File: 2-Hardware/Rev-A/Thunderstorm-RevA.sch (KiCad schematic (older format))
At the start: 16 parts

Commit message: Changed humidity sensor part number to be correct (fixes #1). Updated op-amp circuit to fix incorrect negative terminal wiring (fixes #3). Changed ADC input for humidity sensor to connect Vref to Vcc (fixes #2). Added bulk decoupling capacitor on the Synapse module.
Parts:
- added C4: 0.1uF, ~, symbol C
- A2: renamed from A?; value HIH_3030 -> HIH_5030; symbol HIH_3030 -> HIH_5030
- gave numbers to parts that had none: 15
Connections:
- net labels added: ADC3
- net labels removed: ADC0
- wire segments 89 -> 94
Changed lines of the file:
@@
 LIBS:Sensors
 LIBS:TransistorParts
+LIBS:Thunderstorm-RevA-cache
 EELAYER 27 0
 EELAYER END
@@
 Sheet 1 1
 Title ""
-Date "20 may 2014"
+Date "27 may 2014"
 Rev ""
 Comp ""
@@
 $EndDescr
 $Comp
-L SYNAPSE_RF300 RF?
+L SYNAPSE_RF300 RF1
 U 1 1 537AB6CF
 P 2850 6550
-F 0 "RF?" H 2850 7250 60  0000 C CNN
+F 0 "RF1" H 2850 7250 60  0000 C CNN
 F 1 "SYNAPSE_RF300" H 2900 7350 60  0000 C CNN
 F 2 "~" H 2850 6550 60  0000 C CNN
@@
 $EndComp
 $Comp
-L BATTERY BT?
+L BATTERY BT1
 U 1 1 537AB6DE
 P 9600 4050
-F 0 "BT?" H 9600 4250 50  0000 C CNN
+F 0 "BT1" H 9600 4250 50  0000 C CNN
 F 1 "BATTERY" H 9600 3860 50  0000 C CNN
 F 2 "~" H 9600 4050 60  0000 C CNN
@@
 $EndComp
 $Comp
-L SWITCH_SPDT SW?
+L SWITCH_SPDT SW1
 U 1 1 537AB6ED
 P 10300 4050
-F 0 "SW?" H 10300 4200 50  0000 C CNN
+F 0 "SW1" H 10300 4200 50  0000 C CNN
 F 1 "SWITCH_SPDT" H 10300 3950 50  0000 C CNN
 F 2 "~" H 10300 4050 60  0000 C CNN
@@
 $EndComp
 $Comp
-L GND #PWR?
+L GND #PWR11
 U 1 1 537AB6FC
 P 9200 4150
-F 0 "#PWR?" H 9200 4150 30  0001 C CNN
+F 0 "#PWR11" H 9200 4150 30  0001 C CNN
 F 1 "GND" H 9200 4080 30  0001 C CNN
 F 2 "" H 9200 4150 60  0000 C CNN
@@
 	10600 4000 10600 3950
 $Comp
-L +BATT #PWR?
+L +BATT #PWR14
 U 1 1 537AB71B
 P 10600 3950
-F 0 "#PWR?" H 10600 3900 20  0001 C CNN
+F 0 "#PWR14" H 10600 3900 20  0001 C CNN
 F 1 "+BATT" H 10600 4050 30  0000 C CNN
 F 2 "" H 10600 3950 60  0000 C CNN
@@
 $EndComp
 $Comp
-L +BATT #PWR?
+L +BATT #PWR5
 U 1 1 537AB72A
 P 4050 6000
-F 0 "#PWR?" H 4050 5950 20  0001 C CNN
+F 0 "#PWR5" H 4050 5950 20  0001 C CNN
 F 1 "+BATT" H 4050 6100 30  0000 C CNN
 F 2 "" H 4050 6000 60  0000 C CNN
@@
 	4050 6300 3400 6300
 $Comp
-L GND #PWR?
+L GND #PWR4
 U 1 1 537AB73F
 P 3600 5900
-F 0 "#PWR?" H 3600 5900 30  0001 C CNN
+F 0 "#PWR4" H 3600 5900 30  0001 C CNN
 F 1 "GND" H 3600 5830 30  0001 C CNN
 F 2 "" H 3600 5900 60  0000 C CNN
@@
 $EndComp
 $Comp
-L GND #PWR?
+L GND #PWR3
 U 1 1 537AB74E
 P 2050 5950
-F 0 "#PWR?" H 2050 5950 30  0001 C CNN
+F 0 "#PWR3" H 2050 5950 30  0001 C CNN
 F 1 "GND" H 2050 5880 30  0001 C CNN
 F 2 "" H 2050 5950 60  0000 C CNN
@@
 $EndComp
 $Comp
-L R R?
+L R R3
 U 1 1 537AB784
 P 3750 6100
-F 0 "R?" V 3830 6100 40  0000 C CNN
+F 0 "R3" V 3830 6100 40  0000 C CNN
 F 1 "4.7k" V 3757 6101 40  0000 C CNN
 F 2 "~" V 3680 6100 30  0000 C CNN
@@
 	2050 5900 2050 5950
 $Comp
-L R R?
+L R R1
 U 1 1 537AB7FB
 P 1500 5750
-F 0 "R?" V 1580 5750 40  0000 C CNN
+F 0 "R1" V 1580 5750 40  0000 C CNN
 F 1 "4.7k" V 1507 5751 40  0000 C CNN
 F 2 "~" V 1430 5750 30  0000 C CNN
@@
 $EndComp
 $Comp
-L R R?
+L R R2
 U 1 1 537AB80A
 P 1700 5750
-F 0 "R?" V 1780 5750 40  0000 C CNN
+F 0 "R2" V 1780 5750 40  0000 C CNN
 F 1 "4.7k" V 1707 5751 40  0000 C CNN
 F 2 "~" V 1630 5750 30  0000 C CNN
@@
 $EndComp
 $Comp
-L +BATT #PWR?
+L +BATT #PWR1
 U 1 1 537AB819
 P 1600 5400
-F 0 "#PWR?" H 1600 5350 20  0001 C CNN
+F 0 "#PWR1" H 1600 5350 20  0001 C CNN
 F 1 "+BATT" H 1600 5500 30  0000 C CNN
 F 2 "" H 1600 5400 60  0000 C CNN
@@
 Text Label 1400 6200 2    60   ~ 0
 SCL
-Text Label 1900 6700 2    60   ~ 0
-ADC0
-Wire Wire Line
-	2300 6700 1900 6700
+Text Label 1900 7000 2    60   ~ 0
+ADC3
 Text Label 1900 6800 2    60   ~ 0
 USART_RF_RXI
@@
 	2300 6800 1900 6800
 $Comp
-L M10382 U?
+L M10382 U1
 U 1 1 537AB9A1
 P 9100 2250
-F 0 "U?" H 9100 2300 60  0000 C CNN
+F 0 "U1" H 9100 2300 60  0000 C CNN
 F 1 "M10382" H 9100 2200 60  0000 C CNN
 F 2 "~" H 9100 2250 60  0000 C CNN
@@
 $EndComp
 $Comp
-L GND #PWR?
+L GND #PWR10
 U 1 1 537AB9B0
 P 9100 3050
-F 0 "#PWR?" H 9100 3050 30  0001 C CNN
+F 0 "#PWR10" H 9100 3050 30  0001 C CNN
 F 1 "GND" H 9100 2980 30  0001 C CNN
 F 2 "" H 9100 3050 60  0000 C CNN
@@
 Connection ~ 9550 2950
 $Comp
-L +BATT #PWR?
+L +BATT #PWR9
 U 1 1 537ABBDB
 P 7400 1850
-F 0 "#PWR?" H 7400 1800 20  0001 C CNN
+F 0 "#PWR9" H 7400 1800 20  0001 C CNN
 F 1 "+BATT" H 7400 1950 30  0000 C CNN
 F 2 "" H 7400 1850 60  0000 C CNN
@@
 Connection ~ 7400 2150
 $Comp
-L C C?
+L C C1
 U 1 1 537ABC6A
 P 7400 2650
-F 0 "C?" H 7400 2750 40  0000 L CNN
+F 0 "C1" H 7400 2750 40  0000 L CNN
 F 1 "22pF" H 7406 2565 40  0000 L CNN
 F 2 "~" H 7438 2500 30  0000 C CNN
@@
 Connection ~ 7400 2350
 $Comp
-L C C?
+L C C2
 U 1 1 537ABD23
 P 10750 2250
-F 0 "C?" H 10750 2350 40  0000 L CNN
+F 0 "C2" H 10750 2350 40  0000 L CNN
 F 1 "22pF" H 10756 2165 40  0000 L CNN
 F 2 "~" H 10788 2100 30  0000 C CNN
@@
 	9200 1550 9200 1650
 $Comp
-L HIH_3030 A?
+L HIH_5030 A2
 U 1 1 537AC044
 P 10450 5550
-F 0 "A?" H 10450 5800 60  0000 C CNN
-F 1 "HIH_3030" H 10450 5650 60  0000 C CNN
+F 0 "A2" H 10450 5800 60  0000 C CNN
+F 1 "HIH_5030" H 10450 5650 60  0000 C CNN
 F 2 "" H 10350 5500 60  0000 C CNN
 F 3 "" H 10350 5500 60  0000 C CNN
@@
 $EndComp
 $Comp
-L LM358 U?
+L LM358 U2
 U 1 1 537AC053
 P 9200 6200
-F 0 "U?" H 9150 6400 60  0000 L CNN
+F 0 "U2" H 9150 6400 60  0000 L CNN
 F 1 "LM358" H 9150 5950 60  0000 L CNN
 F 2 "" H 9200 6200 60  0000 C CNN
@@
 	10450 6100 9700 6100
 $Comp
-L R R?
+L R R6
 U 1 1 537AC0BB
 P 10050 6400
-F 0 "R?" V 10130 6400 40  0000 C CNN
+F 0 "R6" V 10130 6400 40  0000 C CNN
 F 1 "68k" V 10057 6401 40  0000 C CNN
 F 2 "~" V 9980 6400 30  0000 C CNN
@@
 	9700 6300 9800 6300
 Wire Wire Line
-	9800 6300 9800 6650
-Wire Wire Line
 	9300 6650 10850 6650
 Wire Wire Line
@@
 Connection ~ 10050 6650
 $Comp
-L GND #PWR?
+L GND #PWR13
 U 1 1 537AC1B6
 P 10050 6750
-F 0 "#PWR?" H 10050 6750 30  0001 C CNN
+F 0 "#PWR13" H 10050 6750 30  0001 C CNN
 F 1 "GND" H 10050 6680 30  0001 C CNN
 F 2 "" H 10050 6750 60  0000 C CNN
@@
 	10050 6650 10050 6750
 $Comp
-L +BATT #PWR?
+L +BATT #PWR15
 U 1 1 537AC216
 P 10850 5800
-F 0 "#PWR?" H 10850 5750 20  0001 C CNN
+F 0 "#PWR15" H 10850 5750 20  0001 C CNN
 F 1 "+BATT" H 10850 5900 30  0000 C CNN
 F 2 "" H 10850 5800 60  0000 C CNN
@@
 $EndComp
 $Comp
-L +BATT #PWR?
+L +BATT #PWR12
 U 1 1 537AC225
 P 9300 5700
-F 0 "#PWR?" H 9300 5650 20  0001 C CNN
+F 0 "#PWR12" H 9300 5650 20  0001 C CNN
 F 1 "+BATT" H 9300 5800 30  0000 C CNN
 F 2 "" H 9300 5700 60  0000 C CNN
@@
 Wire Wire Line
 	9300 6600 9300 6650
-Connection ~ 9800 6650
 Wire Wire Line
 	10050 6150 10050 6100
@@
 	10850 5800 10850 6150
 Text Label 8600 6200 2    60   ~ 0
-ADC0
+ADC3
 Wire Wire Line
 	8700 6200 8600 6200
@@
 Power
 $Comp
-L C C?
+L C C3
 U 1 1 537AC660
 P 10850 6350
-F 0 "C?" H 10850 6450 40  0000 L CNN
+F 0 "C3" H 10850 6450 40  0000 L CNN
 F 1 "0.1uF" H 10856 6265 40  0000 L CNN
 F 2 "~" H 10888 6200 30  0000 C CNN
@@
 Connection ~ 10850 5850
 $Comp
-L LPS331AP A?
+L LPS331AP A1
 U 1 1 537ACB3D
 P 6750 6200
-F 0 "A?" H 6300 6700 60  0000 C CNN
+F 0 "A1" H 6300 6700 60  0000 C CNN
 F 1 "LPS331AP" H 7200 5700 60  0000 C CNN
 F 2 "" H 6900 6000 60  0000 C CNN
@@
 $EndComp
 $Comp
-L GND #PWR?
+L GND #PWR8
 U 1 1 537ACB4C
 P 6750 7050
-F 0 "#PWR?" H 6750 7050 30  0001 C CNN
+F 0 "#PWR8" H 6750 7050 30  0001 C CNN
 F 1 "GND" H 6750 6980 30  0001 C CNN
 F 2 "" H 6750 7050 60  0000 C CNN
@@
 Connection ~ 6650 6950
 $Comp
-L R R?
+L R R4
 U 1 1 537ACDDA
 P 7550 5750
-F 0 "R?" V 7630 5750 40  0000 C CNN
+F 0 "R4" V 7630 5750 40  0000 C CNN
 F 1 "4.7k" V 7557 5751 40  0000 C CNN
 F 2 "~" V 7480 5750 30  0000 C CNN
@@
 	6750 5350 6750 5650
 $Comp
-L +BATT #PWR?
+L +BATT #PWR7
 U 1 1 537ACEB8
 P 6750 5350
-F 0 "#PWR?" H 6750 5300 20  0001 C CNN
+F 0 "#PWR7" H 6750 5300 20  0001 C CNN
 F 1 "+BATT" H 6750 5450 30  0000 C CNN
 F 2 "" H 6750 5350 60  0000 C CNN
@@
 Connection ~ 6950 6950
 $Comp
-L R R?
+L R R5
 U 1 1 537AD31D
 P 7650 6650
-F 0 "R?" V 7730 6650 40  0000 C CNN
+F 0 "R5" V 7730 6650 40  0000 C CNN
 F 1 "4.7k" V 7657 6651 40  0000 C CNN
 F 2 "~" V 7580 6650 30  0000 C CNN
@@
 Wire Notes Line
 	6950 3350 6950 500
+Wire Wire Line
+	9800 6300 9800 6750
+Wire Wire Line
+	9800 6750 8650 6750
+Wire Wire Line
+	8650 6750 8650 6200
+Connection ~ 8650 6200
+$Comp
+L +BATT #PWR2
+U 1 1 53851E13
+P 1800 6650
+F 0 "#PWR2" H 1800 6600 20  0001 C CNN
+F 1 "+BATT" H 1800 6750 30  0000 C CNN
+F 2 "" H 1800 6650 60  0000 C CNN
+F 3 "" H 1800 6650 60  0000 C CNN
+	1    1800 6650
+	1    0    0    -1
+$EndComp
+Wire Wire Line
+	2300 6700 1800 6700
+Wire Wire Line
+	1800 6700 1800 6650
+Wire Wire Line
+	1900 7000 2300 7000
+$Comp
+L C C4
+U 1 1 53852370
+P 4050 6500
+F 0 "C4" H 4050 6600 40  0000 L CNN
+F 1 "0.1uF" H 4056 6415 40  0000 L CNN
+F 2 "~" H 4088 6350 30  0000 C CNN
+F 3 "~" H 4050 6500 60  0000 C CNN
+	1    4050 6500
+	1    0    0    -1
+$EndComp
+$Comp
+L GND #PWR6
+U 1 1 5385237F
+P 4050 6800
+F 0 "#PWR6" H 4050 6800 30  0001 C CNN
+F 1 "GND" H 4050 6730 30  0001 C CNN
+F 2 "" H 4050 6800 60  0000 C CNN
+F 3 "" H 4050 6800 60  0000 C CNN
+	1    4050 6800
+	1    0    0    -1
+$EndComp
+Wire Wire Line
+	4050 6700 4050 6800
 $EndSCHEMATC

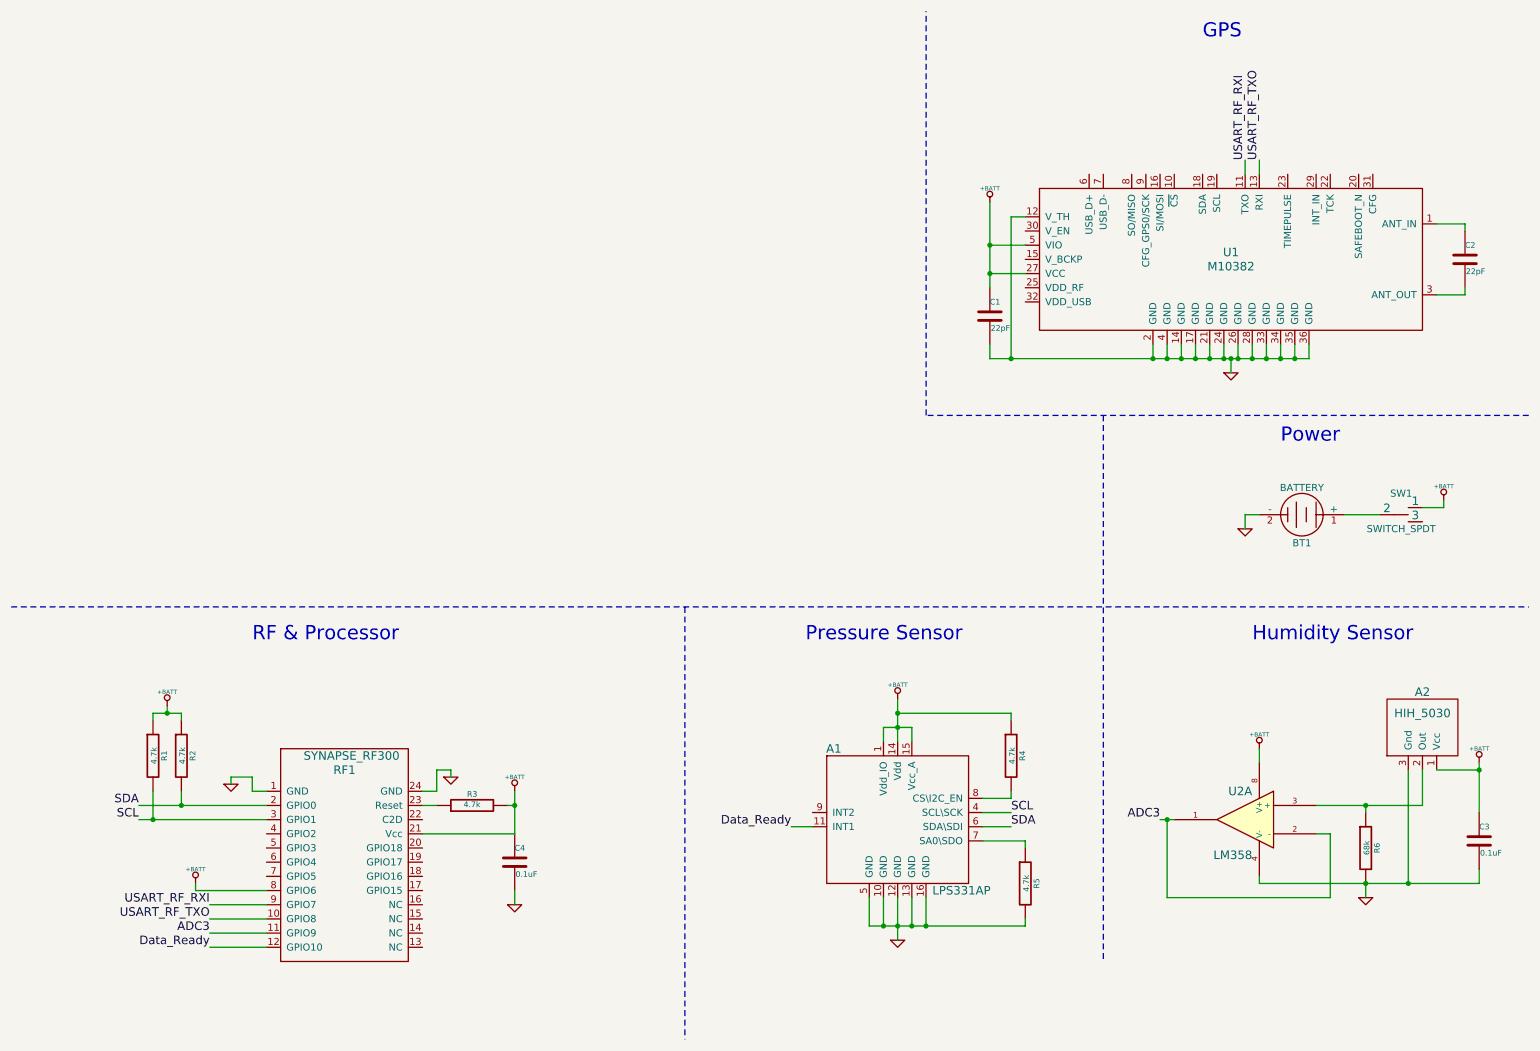
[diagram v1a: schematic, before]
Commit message: Added LEDs for power and diagnostics. (Fixes #4).
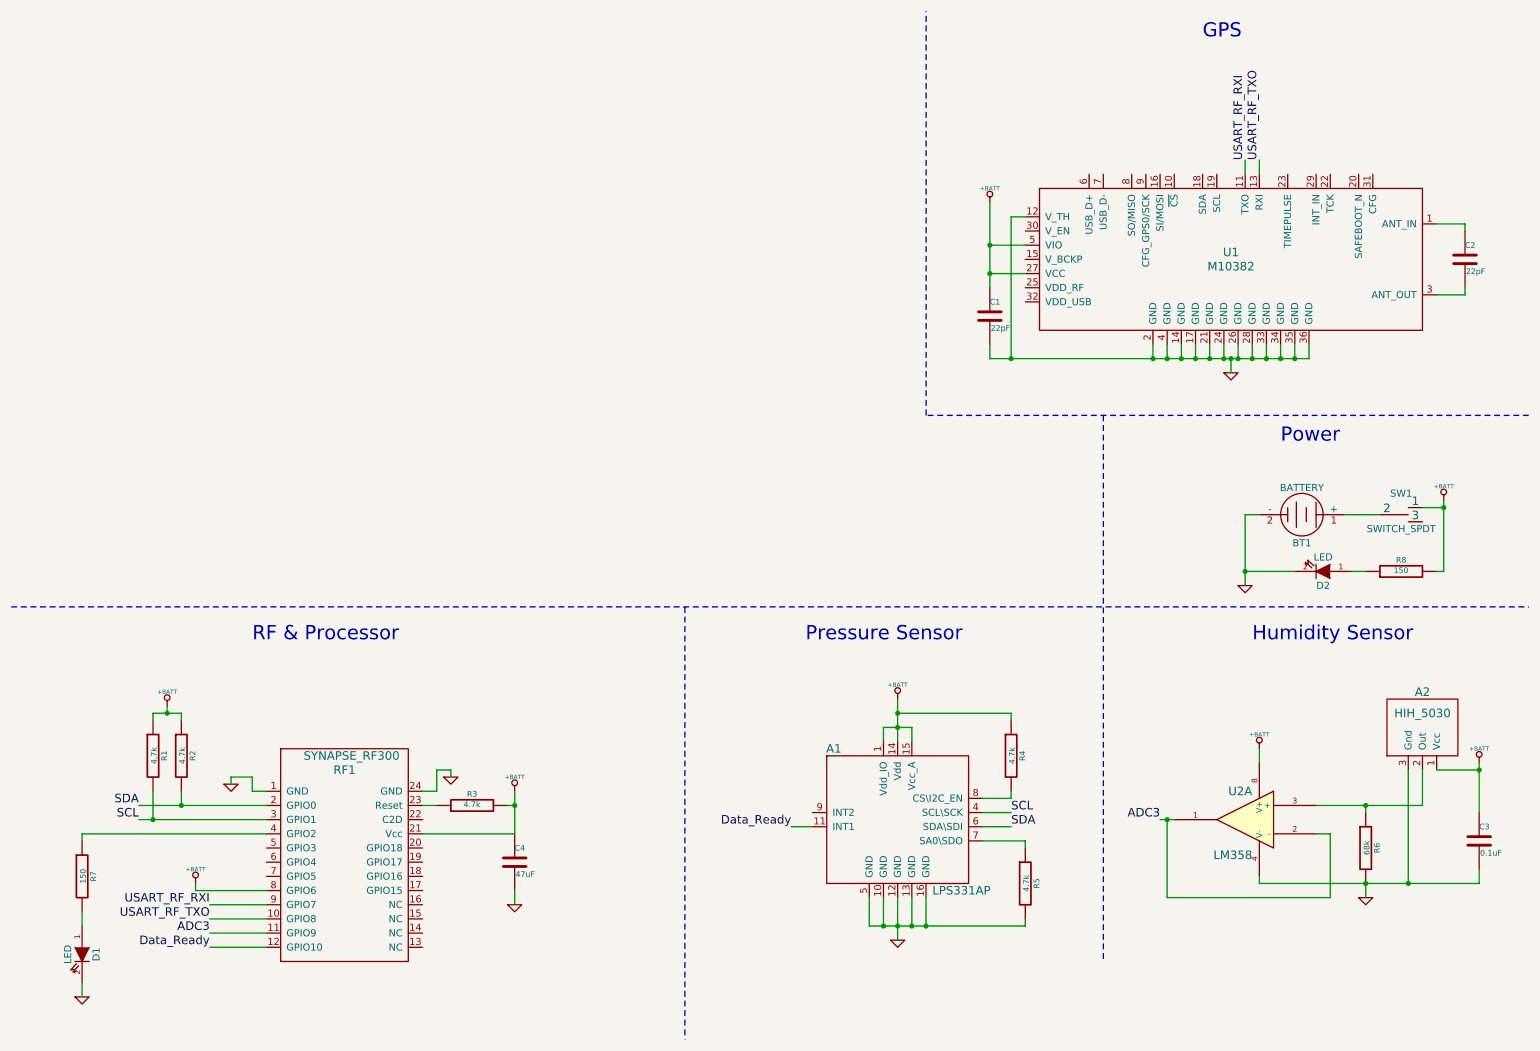
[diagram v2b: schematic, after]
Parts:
- added D1, D2: LED, ~, symbol LED
- added R7, R8: 150, ~, symbol R
- C4: value 0.1uF -> 47uF
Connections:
- net +BATT: now also R8.2
- net GND: now also D1.2 (K), D2.2 (K)
- net at RF1.4 (GPIO2): now also R7.1
- new net: D2.1 (A), R8.1
- new net: D1.1 (A), R7.2
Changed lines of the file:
@@
 Sheet 1 1
 Title ""
-Date "27 may 2014"
+Date "28 may 2014"
 Rev ""
 Comp ""
@@
 $EndComp
 $Comp
-L GND #PWR11
+L GND #PWR12
 U 1 1 537AB6FC
-P 9200 4150
-F 0 "#PWR11" H 9200 4150 30  0001 C CNN
-F 1 "GND" H 9200 4080 30  0001 C CNN
-F 2 "" H 9200 4150 60  0000 C CNN
-F 3 "" H 9200 4150 60  0000 C CNN
-	1    9200 4150
+P 9200 4550
+F 0 "#PWR12" H 9200 4550 30  0001 C CNN
+F 1 "GND" H 9200 4480 30  0001 C CNN
+F 2 "" H 9200 4550 60  0000 C CNN
+F 3 "" H 9200 4550 60  0000 C CNN
+	1    9200 4550
 	1    0    0    -1
 $EndComp
@@
 	9300 4050 9200 4050
 Wire Wire Line
-	9200 4050 9200 4150
+	9200 4050 9200 4550
 Wire Wire Line
 	9900 4050 10150 4050
@@
 	10450 4000 10600 4000
 Wire Wire Line
-	10600 4000 10600 3950
-$Comp
-L +BATT #PWR14
+	10600 3950 10600 4450
+$Comp
+L +BATT #PWR15
 U 1 1 537AB71B
 P 10600 3950
-F 0 "#PWR14" H 10600 3900 20  0001 C CNN
+F 0 "#PWR15" H 10600 3900 20  0001 C CNN
 F 1 "+BATT" H 10600 4050 30  0000 C CNN
 F 2 "" H 10600 3950 60  0000 C CNN
@@
 $EndComp
 $Comp
-L +BATT #PWR5
+L +BATT #PWR6
 U 1 1 537AB72A
 P 4050 6000
-F 0 "#PWR5" H 4050 5950 20  0001 C CNN
+F 0 "#PWR6" H 4050 5950 20  0001 C CNN
 F 1 "+BATT" H 4050 6100 30  0000 C CNN
 F 2 "" H 4050 6000 60  0000 C CNN
@@
 	4050 6300 3400 6300
 $Comp
-L GND #PWR4
+L GND #PWR5
 U 1 1 537AB73F
 P 3600 5900
-F 0 "#PWR4" H 3600 5900 30  0001 C CNN
+F 0 "#PWR5" H 3600 5900 30  0001 C CNN
 F 1 "GND" H 3600 5830 30  0001 C CNN
 F 2 "" H 3600 5900 60  0000 C CNN
@@
 $EndComp
 $Comp
-L GND #PWR3
+L GND #PWR4
 U 1 1 537AB74E
 P 2050 5950
-F 0 "#PWR3" H 2050 5950 30  0001 C CNN
+F 0 "#PWR4" H 2050 5950 30  0001 C CNN
 F 1 "GND" H 2050 5880 30  0001 C CNN
 F 2 "" H 2050 5950 60  0000 C CNN
@@
 $EndComp
 $Comp
-L +BATT #PWR1
+L +BATT #PWR2
 U 1 1 537AB819
 P 1600 5400
-F 0 "#PWR1" H 1600 5350 20  0001 C CNN
+F 0 "#PWR2" H 1600 5350 20  0001 C CNN
 F 1 "+BATT" H 1600 5500 30  0000 C CNN
 F 2 "" H 1600 5400 60  0000 C CNN
@@
 $EndComp
 $Comp
-L GND #PWR10
+L GND #PWR11
 U 1 1 537AB9B0
 P 9100 3050
-F 0 "#PWR10" H 9100 3050 30  0001 C CNN
+F 0 "#PWR11" H 9100 3050 30  0001 C CNN
 F 1 "GND" H 9100 2980 30  0001 C CNN
 F 2 "" H 9100 3050 60  0000 C CNN
@@
 Connection ~ 9550 2950
 $Comp
-L +BATT #PWR9
+L +BATT #PWR10
 U 1 1 537ABBDB
 P 7400 1850
-F 0 "#PWR9" H 7400 1800 20  0001 C CNN
+F 0 "#PWR10" H 7400 1800 20  0001 C CNN
 F 1 "+BATT" H 7400 1950 30  0000 C CNN
 F 2 "" H 7400 1850 60  0000 C CNN
@@
 $EndComp
 Wire Wire Line
-	10450 5850 10450 6100
-Wire Wire Line
-	10450 6100 9700 6100
+	10450 6100 10450 5850
+Wire Wire Line
+	9700 6100 10450 6100
 $Comp
 L R R6
@@
 Connection ~ 10050 6650
 $Comp
-L GND #PWR13
+L GND #PWR14
 U 1 1 537AC1B6
 P 10050 6750
-F 0 "#PWR13" H 10050 6750 30  0001 C CNN
+F 0 "#PWR14" H 10050 6750 30  0001 C CNN
 F 1 "GND" H 10050 6680 30  0001 C CNN
 F 2 "" H 10050 6750 60  0000 C CNN
@@
 	10050 6650 10050 6750
 $Comp
-L +BATT #PWR15
+L +BATT #PWR16
 U 1 1 537AC216
 P 10850 5800
-F 0 "#PWR15" H 10850 5750 20  0001 C CNN
+F 0 "#PWR16" H 10850 5750 20  0001 C CNN
 F 1 "+BATT" H 10850 5900 30  0000 C CNN
 F 2 "" H 10850 5800 60  0000 C CNN
@@
 $EndComp
 $Comp
-L +BATT #PWR12
+L +BATT #PWR13
 U 1 1 537AC225
 P 9300 5700
-F 0 "#PWR12" H 9300 5650 20  0001 C CNN
+F 0 "#PWR13" H 9300 5650 20  0001 C CNN
 F 1 "+BATT" H 9300 5800 30  0000 C CNN
 F 2 "" H 9300 5700 60  0000 C CNN
@@
 ADC3
 Wire Wire Line
-	8700 6200 8600 6200
+	8600 6200 8700 6200
 Text Notes 9250 4950 0    100  ~ 0
 Humidity Sensor
@@
 $EndComp
 $Comp
-L GND #PWR8
+L GND #PWR9
 U 1 1 537ACB4C
 P 6750 7050
-F 0 "#PWR8" H 6750 7050 30  0001 C CNN
+F 0 "#PWR9" H 6750 7050 30  0001 C CNN
 F 1 "GND" H 6750 6980 30  0001 C CNN
 F 2 "" H 6750 7050 60  0000 C CNN
@@
 	6750 5350 6750 5650
 $Comp
-L +BATT #PWR7
+L +BATT #PWR8
 U 1 1 537ACEB8
 P 6750 5350
-F 0 "#PWR7" H 6750 5300 20  0001 C CNN
+F 0 "#PWR8" H 6750 5300 20  0001 C CNN
 F 1 "+BATT" H 6750 5450 30  0000 C CNN
 F 2 "" H 6750 5350 60  0000 C CNN
@@
 Connection ~ 8650 6200
 $Comp
-L +BATT #PWR2
+L +BATT #PWR3
 U 1 1 53851E13
 P 1800 6650
-F 0 "#PWR2" H 1800 6600 20  0001 C CNN
+F 0 "#PWR3" H 1800 6600 20  0001 C CNN
 F 1 "+BATT" H 1800 6750 30  0000 C CNN
 F 2 "" H 1800 6650 60  0000 C CNN
@@
 P 4050 6500
 F 0 "C4" H 4050 6600 40  0000 L CNN
-F 1 "0.1uF" H 4056 6415 40  0000 L CNN
+F 1 "47uF" H 4056 6415 40  0000 L CNN
 F 2 "~" H 4088 6350 30  0000 C CNN
 F 3 "~" H 4050 6500 60  0000 C CNN
@@
 $EndComp
 $Comp
-L GND #PWR6
+L GND #PWR7
 U 1 1 5385237F
 P 4050 6800
-F 0 "#PWR6" H 4050 6800 30  0001 C CNN
+F 0 "#PWR7" H 4050 6800 30  0001 C CNN
 F 1 "GND" H 4050 6730 30  0001 C CNN
 F 2 "" H 4050 6800 60  0000 C CNN
@@
 Wire Wire Line
 	4050 6700 4050 6800
+$Comp
+L R R8
+U 1 1 538674D3
+P 10300 4450
+F 0 "R8" V 10380 4450 40  0000 C CNN
+F 1 "150" V 10307 4451 40  0000 C CNN
+F 2 "~" V 10230 4450 30  0000 C CNN
+F 3 "~" H 10300 4450 30  0000 C CNN
+	1    10300 4450
+	0    -1   -1   0
+$EndComp
+$Comp
+L LED D2
+U 1 1 538674E2
+P 9750 4450
+F 0 "D2" H 9750 4550 50  0000 C CNN
+F 1 "LED" H 9750 4350 50  0000 C CNN
+F 2 "~" H 9750 4450 60  0000 C CNN
+F 3 "~" H 9750 4450 60  0000 C CNN
+	1    9750 4450
+	-1   0    0    1
+$EndComp
+Wire Wire Line
+	10600 4450 10550 4450
+Connection ~ 10600 4000
+Wire Wire Line
+	10050 4450 9950 4450
+Wire Wire Line
+	9550 4450 9200 4450
+Connection ~ 9200 4450
+$Comp
+L LED D1
+U 1 1 538677A9
+P 1000 7150
+F 0 "D1" H 1000 7250 50  0000 C CNN
+F 1 "LED" H 1000 7050 50  0000 C CNN
+F 2 "~" H 1000 7150 60  0000 C CNN
+F 3 "~" H 1000 7150 60  0000 C CNN
+	1    1000 7150
+	0    1    1    0
+$EndComp
+$Comp
+L R R7
+U 1 1 538677B8
+P 1000 6600
+F 0 "R7" V 1080 6600 40  0000 C CNN
+F 1 "150" V 1007 6601 40  0000 C CNN
+F 2 "~" V 930 6600 30  0000 C CNN
+F 3 "~" H 1000 6600 30  0000 C CNN
+	1    1000 6600
+	1    0    0    -1
+$EndComp
+$Comp
+L GND #PWR1
+U 1 1 538677C7
+P 1000 7450
+F 0 "#PWR1" H 1000 7450 30  0001 C CNN
+F 1 "GND" H 1000 7380 30  0001 C CNN
+F 2 "" H 1000 7450 60  0000 C CNN
+F 3 "" H 1000 7450 60  0000 C CNN
+	1    1000 7450
+	1    0    0    -1
+$EndComp
+Wire Wire Line
+	1000 7350 1000 7450
+Wire Wire Line
+	1000 6850 1000 6950
+Wire Wire Line
+	2300 6300 1000 6300
+Wire Wire Line
+	1000 6300 1000 6350
 $EndSCHEMATC
